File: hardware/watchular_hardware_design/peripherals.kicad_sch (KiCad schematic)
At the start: 51 parts, among them J3 TSW-116-07-H-S, J4 TSW-116-07-H-S, Q1 BSS123, Q2 BSS123, Q3 BSS123, Q4 BSS123

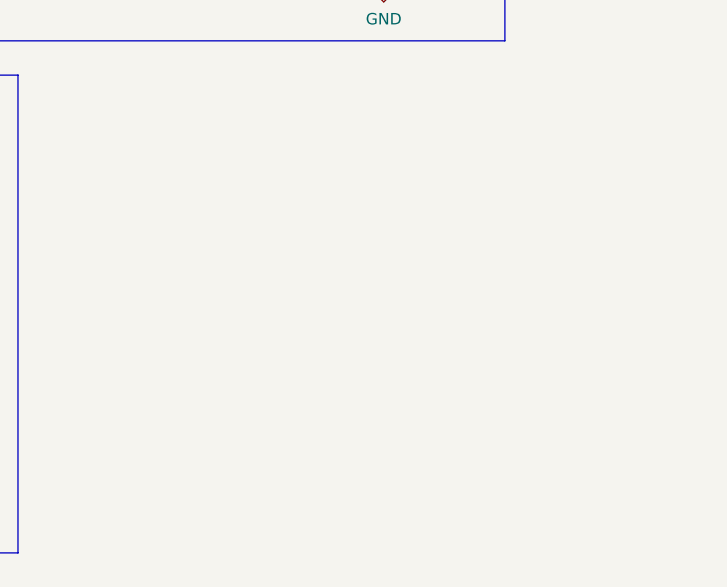
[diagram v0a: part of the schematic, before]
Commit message: Added mouting holes and assigned footprints.
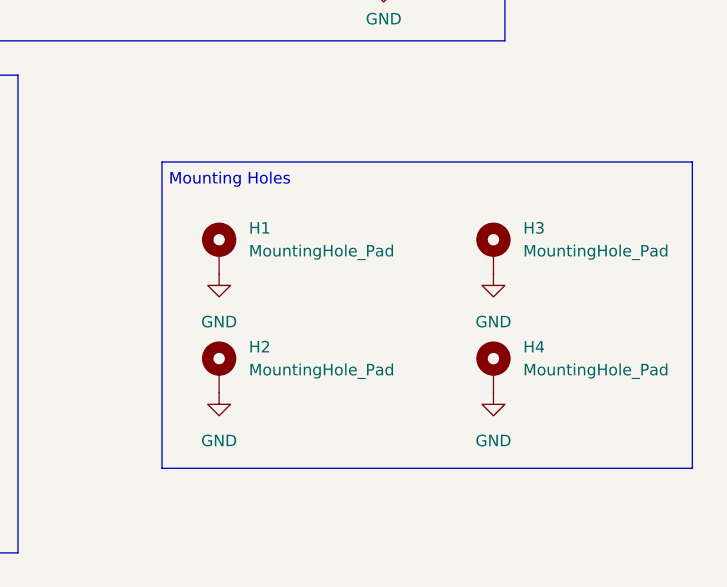
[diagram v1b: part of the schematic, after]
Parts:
- added H1, H2, H3, H4: MountingHole_Pad, MountingHole:MountingHole_4.3mm_M4_Pad_Via, symbol Mechanical:MountingHole_Pad
- J3, J4: footprint SAMTEC_TSW-116-07-H-S -> header-TSW-116-07-H-S:SAMTEC_TSW-116-07-H-S
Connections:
- net GND: now also H1.1, H2.1, H3.1, H4.1
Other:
- note added: "Mounting Holes"
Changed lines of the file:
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@@
+    (stroke (width 0) (type default) (color 0 0 0 0))
+  )
+  (polyline (pts (xy 224.028 149.606) (xy 224.028 115.57))
     (stroke (width 0) (type default) (color 0 0 0 0))
   )
@@
     (stroke (width 0) (type default) (color 0 0 0 0))
   )
+  (polyline (pts (xy 224.028 115.57) (xy 282.956 115.57))
+    (stroke (width 0) (type default) (color 0 0 0 0))
+  )
   (wire (pts (xy 35.814 58.928) (xy 39.624 58.928))
     (stroke (width 0) (type default) (color 0 0 0 0))
@@
     (stroke (width 0) (type default) (color 0 0 0 0))
   )
+  (polyline (pts (xy 282.956 149.606) (xy 224.028 149.606))
+    (stroke (width 0) (type default) (color 0 0 0 0))
+  )
   (polyline (pts (xy 76.454 116.84) (xy 76.454 160.782))
     (stroke (width 0) (type default) (color 0 0 0 0))
@@
   )
   (wire (pts (xy 248.666 69.85) (xy 248.666 78.105))
+    (stroke (width 0) (type default) (color 0 0 0 0))
+  )
+  (polyline (pts (xy 282.956 115.57) (xy 282.956 149.606))
     (stroke (width 0) (type default) (color 0 0 0 0))
   )
@@
   )
   (text "Buttons" (at 18.796 119.888 0)
+    (effects (font (size 1.27 1.27)) (justify left bottom))
+  )
+  (text "Mounting Holes" (at 224.79 118.364 0)
     (effects (font (size 1.27 1.27)) (justify left bottom))
   )
@@
     )
   )
+  (symbol (lib_id "power:GND") (at 230.378 141.224 0) (unit 1)
+    (in_bom yes) (on_board yes) (fields_autoplaced)
+    (property "Reference" "#PWR053" (id 0) (at 230.378 147.574 0)
+      (effects (font (size 1.27 1.27)) hide)
+    )
+    (property "Value" "GND" (id 1) (at 230.378 146.558 0))
+    (property "Footprint" "" (id 2) (at 230.378 141.224 0)
+      (effects (font (size 1.27 1.27)) hide)
+    )
+    (property "Datasheet" "" (id 3) (at 230.378 141.224 0)
+      (effects (font (size 1.27 1.27)) hide)
+    )
+    (pin "1")
+  )
   (symbol (lib_id "BSS123:BSS123") (at 201.422 89.916 0) (unit 1)
     (in_bom yes) (on_board yes) (fields_autoplaced)
@@
     (pin "2")
   )
+  (symbol (lib_id "power:GND") (at 260.858 128.016 0) (unit 1)
+    (in_bom yes) (on_board yes) (fields_autoplaced)
+    (property "Reference" "#PWR054" (id 0) (at 260.858 134.366 0)
+      (effects (font (size 1.27 1.27)) hide)
+    )
+    (property "Value" "GND" (id 1) (at 260.858 133.35 0))
+    (property "Footprint" "" (id 2) (at 260.858 128.016 0)
+      (effects (font (size 1.27 1.27)) hide)
+    )
+    (property "Datasheet" "" (id 3) (at 260.858 128.016 0)
+      (effects (font (size 1.27 1.27)) hide)
+    )
+    (pin "1")
+  )
   (symbol (lib_id "Device:LED") (at 191.262 42.926 180) (unit 1)
     (in_bom yes) (on_board yes)
@@
     (pin "2")
   )
+  (symbol (lib_id "Mechanical:MountingHole_Pad") (at 230.378 125.476 0) (unit 1)
+    (in_bom yes) (on_board yes) (fields_autoplaced)
+    (property "Reference" "H1" (id 0) (at 233.68 122.9359 0)
+      (effects (font (size 1.27 1.27)) (justify left))
+    )
+    (property "Value" "MountingHole_Pad" (id 1) (at 233.68 125.4759 0)
+      (effects (font (size 1.27 1.27)) (justify left))
+    )
+    (property "Footprint" "MountingHole:MountingHole_4.3mm_M4_Pad_Via" (id 2) (at 230.378 125.476 0)
+      (effects (font (size 1.27 1.27)) hide)
+    )
+    (property "Datasheet" "~" (id 3) (at 230.378 125.476 0)
+      (effects (font (size 1.27 1.27)) hide)
+    )
+    (pin "1")
+  )
   (symbol (lib_id "power:GND") (at 172.974 46.228 0) (unit 1)
     (in_bom yes) (on_board yes) (fields_autoplaced)
@@
     (pin "2")
   )
+  (symbol (lib_id "Mechanical:MountingHole_Pad") (at 260.858 125.476 0) (unit 1)
+    (in_bom yes) (on_board yes) (fields_autoplaced)
+    (property "Reference" "H3" (id 0) (at 264.16 122.9359 0)
+      (effects (font (size 1.27 1.27)) (justify left))
+    )
+    (property "Value" "MountingHole_Pad" (id 1) (at 264.16 125.4759 0)
+      (effects (font (size 1.27 1.27)) (justify left))
+    )
+    (property "Footprint" "MountingHole:MountingHole_4.3mm_M4_Pad_Via" (id 2) (at 260.858 125.476 0)
+      (effects (font (size 1.27 1.27)) hide)
+    )
+    (property "Datasheet" "~" (id 3) (at 260.858 125.476 0)
+      (effects (font (size 1.27 1.27)) hide)
+    )
+    (pin "1")
+  )
   (symbol (lib_id "Device:LED") (at 191.262 60.706 180) (unit 1)
     (in_bom yes) (on_board yes)
@@
       (effects (font (size 1.27 1.27)) (justify left) hide)
     )
-    (property "Footprint" "SAMTEC_TSW-116-07-H-S" (id 2) (at 140.462 137.668 0)
+    (property "Footprint" "header-TSW-116-07-H-S:SAMTEC_TSW-116-07-H-S" (id 2) (at 140.462 137.668 0)
       (effects (font (size 1.27 1.27)) (justify left bottom) hide)
     )
@@
     (pin "2")
   )
+  (symbol (lib_id "power:GND") (at 260.858 141.224 0) (unit 1)
+    (in_bom yes) (on_board yes) (fields_autoplaced)
+    (property "Reference" "#PWR055" (id 0) (at 260.858 147.574 0)
+      (effects (font (size 1.27 1.27)) hide)
+    )
+    (property "Value" "GND" (id 1) (at 260.858 146.558 0))
+    (property "Footprint" "" (id 2) (at 260.858 141.224 0)
+      (effects (font (size 1.27 1.27)) hide)
+    )
+    (property "Datasheet" "" (id 3) (at 260.858 141.224 0)
+      (effects (font (size 1.27 1.27)) hide)
+    )
+    (pin "1")
+  )
+  (symbol (lib_id "power:GND") (at 230.378 128.016 0) (unit 1)
+    (in_bom yes) (on_board yes) (fields_autoplaced)
+    (property "Reference" "#PWR052" (id 0) (at 230.378 134.366 0)
+      (effects (font (size 1.27 1.27)) hide)
+    )
+    (property "Value" "GND" (id 1) (at 230.378 133.35 0))
+    (property "Footprint" "" (id 2) (at 230.378 128.016 0)
+      (effects (font (size 1.27 1.27)) hide)
+    )
+    (property "Datasheet" "" (id 3) (at 230.378 128.016 0)
+      (effects (font (size 1.27 1.27)) hide)
+    )
+    (pin "1")
+  )
   (symbol (lib_id "Device:R_Small_US") (at 33.274 50.038 90) (unit 1)
     (in_bom yes) (on_board yes)
@@
     (pin "1")
     (pin "2")
+  )
+  (symbol (lib_id "Mechanical:MountingHole_Pad") (at 230.378 138.684 0) (unit 1)
+    (in_bom yes) (on_board yes) (fields_autoplaced)
+    (property "Reference" "H2" (id 0) (at 233.68 136.1439 0)
+      (effects (font (size 1.27 1.27)) (justify left))
+    )
+    (property "Value" "MountingHole_Pad" (id 1) (at 233.68 138.6839 0)
+      (effects (font (size 1.27 1.27)) (justify left))
+    )
+    (property "Footprint" "MountingHole:MountingHole_4.3mm_M4_Pad_Via" (id 2) (at 230.378 138.684 0)
+      (effects (font (size 1.27 1.27)) hide)
+    )
+    (property "Datasheet" "~" (id 3) (at 230.378 138.684 0)
+      (effects (font (size 1.27 1.27)) hide)
+    )
+    (pin "1")
   )
   (symbol (lib_id "power:GND") (at 201.422 94.996 0) (unit 1)
@@
     (pin "2")
   )
+  (symbol (lib_id "Mechanical:MountingHole_Pad") (at 260.858 138.684 0) (unit 1)
+    (in_bom yes) (on_board yes) (fields_autoplaced)
+    (property "Reference" "H4" (id 0) (at 264.16 136.1439 0)
+      (effects (font (size 1.27 1.27)) (justify left))
+    )
+    (property "Value" "MountingHole_Pad" (id 1) (at 264.16 138.6839 0)
+      (effects (font (size 1.27 1.27)) (justify left))
+    )
+    (property "Footprint" "MountingHole:MountingHole_4.3mm_M4_Pad_Via" (id 2) (at 260.858 138.684 0)
+      (effects (font (size 1.27 1.27)) hide)
+    )
+    (property "Datasheet" "~" (id 3) (at 260.858 138.684 0)
+      (effects (font (size 1.27 1.27)) hide)
+    )
+    (pin "1")
+  )
   (symbol (lib_id "Device:LED") (at 238.506 60.96 180) (unit 1)
     (in_bom yes) (on_board yes)
@@
       (effects (font (size 1.27 1.27)) (justify left) hide)
     )
-    (property "Footprint" "SAMTEC_TSW-116-07-H-S" (id 2) (at 198.12 137.668 0)
+    (property "Footprint" "header-TSW-116-07-H-S:SAMTEC_TSW-116-07-H-S" (id 2) (at 198.12 137.668 0)
       (effects (font (size 1.27 1.27)) (justify left bottom) hide)
     )

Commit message: Bottom side elements first arrangement.
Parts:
- H1, H2, H3, H4: footprint MountingHole:MountingHole_4.3mm_M4_Pad_Via -> MountingHole:MountingHole_2.2mm_M2_Pad_Via
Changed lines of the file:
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@@
       (effects (font (size 1.27 1.27)) (justify left))
     )
-    (property "Footprint" "MountingHole:MountingHole_4.3mm_M4_Pad_Via" (id 2) (at 230.378 125.476 0)
+    (property "Footprint" "MountingHole:MountingHole_2.2mm_M2_Pad_Via" (id 2) (at 230.378 125.476 0)
       (effects (font (size 1.27 1.27)) hide)
     )
@@
       (effects (font (size 1.27 1.27)) (justify left))
     )
-    (property "Footprint" "MountingHole:MountingHole_4.3mm_M4_Pad_Via" (id 2) (at 260.858 125.476 0)
+    (property "Footprint" "MountingHole:MountingHole_2.2mm_M2_Pad_Via" (id 2) (at 260.858 125.476 0)
       (effects (font (size 1.27 1.27)) hide)
     )
@@
       (effects (font (size 1.27 1.27)) (justify left))
     )
-    (property "Footprint" "MountingHole:MountingHole_4.3mm_M4_Pad_Via" (id 2) (at 230.378 138.684 0)
+    (property "Footprint" "MountingHole:MountingHole_2.2mm_M2_Pad_Via" (id 2) (at 230.378 138.684 0)
       (effects (font (size 1.27 1.27)) hide)
     )
@@
       (effects (font (size 1.27 1.27)) (justify left))
     )
-    (property "Footprint" "MountingHole:MountingHole_4.3mm_M4_Pad_Via" (id 2) (at 260.858 138.684 0)
-      (effects (font (size 1.27 1.27)) hide)
-    )
+    (property "Footprint" "MountingHole:MountingHole_2.2mm_M2_Pad_Via" (id 2) (at 260.858 138.684 0)
+      (effects (font (size 1.27 1.27)) hide)
+    )

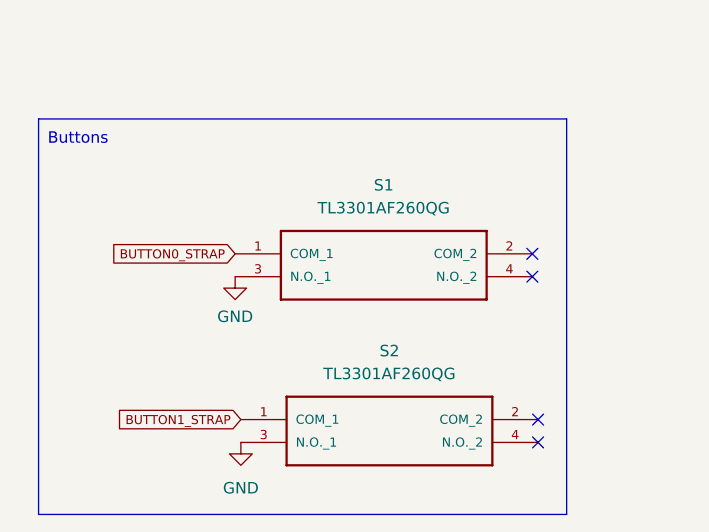
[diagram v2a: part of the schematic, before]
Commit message: Imported a bit smaller buttons.
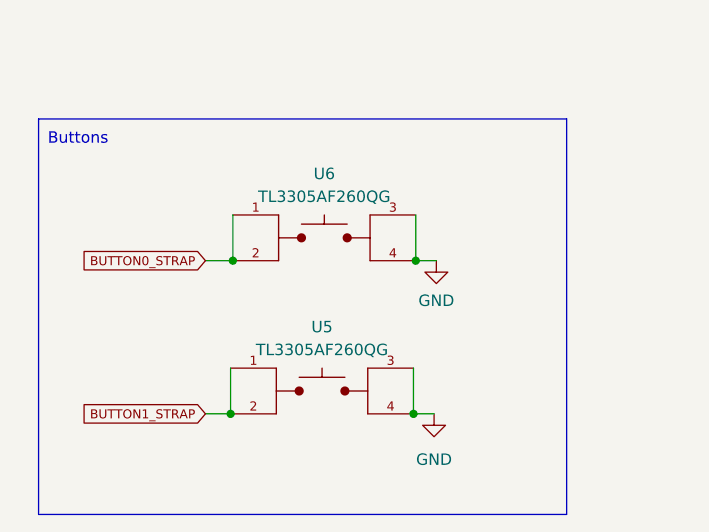
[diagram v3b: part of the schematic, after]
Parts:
- removed S1, S2: TL3301AF260QG, switch-TL3301AF260QG:TL3301AF260QG, symbol TL3301AF260QG:TL3301AF260QG
- added U5, U6: TL3305AF260QG, button_TL3305AF260QG:SW_TL3305AF260QG, symbol TL3305AF260QG:TL3305AF260QG
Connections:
- net BUTTON0_STRAP: now also U6.1, U6.2
- net BUTTON1_STRAP: now also U5.1, U5.2
- net GND: now also U5.3, U5.4, U6.3, U6.4
- no-connect marks 4 -> 0

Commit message: Locked the first digit.
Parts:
- removed H3, H4: MountingHole_Pad, MountingHole:MountingHole_2.2mm_M2_Pad_Via, symbol Mechanical:MountingHole_Pad
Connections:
- net +5V: now also J3.15; no longer J3.01
- net +BATT: now also J4.16; no longer J4.01
- net A_MCU: now also J3.02; no longer J3.04
- net BUTTON0_STRAP: now also J3.04; no longer J3.06
- net BUTTON1_STRAP: now also J3.12; no longer J3.14
- net B_MCU: now also J3.03; no longer J3.05
- net CHIP_EN: now also J3.05; no longer J3.07
- net CS-memory: now also J4.11; no longer J4.12
- net C_MCU: now also J3.07; no longer J3.09
- net DI-memory: now also J4.09; no longer J4.10
- net DIGI0: now also J4.04; no longer J4.05
- net DIGI1: now also J3.06; no longer J3.08
- net DIGI2: now also J3.14; no longer J3.16
- net DIGI3_STRAP: now also J3.13; no longer J3.15
- net DIV0-with_no_internal_flash_ONLY: now also J4.13; no longer J4.14
- net DIV1-with_no_internal_flash_ONLY: now also J4.12; no longer J4.13
- net DO-memory: now also J4.08; no longer J4.09
- net D_MCU: now also J3.08; no longer J3.10
- net E_MCU: now also J3.10; no longer J3.12
- net F_MCU: now also J3.11; no longer J3.13
- net GND: now also J3.16; no longer J3.02
- net GPIO11-to_breakout-TEST_ONLY: now also J4.14; no longer J4.15
- net G_MCU: now also J4.05; no longer J4.06
- net SPICLK-memory: now also J4.10; no longer J4.11
- net USB_D+: now also J4.06; no longer J4.07
- net USB_D-: now also J4.07; no longer J4.08
- net VDD3P3: now also J3.01; no longer J3.03
- net VDD3P3_CPU: now also J4.15; no longer J4.16
- net VDD3P3_RTC: now also J3.09; no longer J3.11
- net VDDA: now also J4.01; no longer J4.02
- net XTAL_N: now also J4.03; no longer J4.04
- net XTAL_P: now also J4.02; no longer J4.03

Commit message: Figuring out the top side...
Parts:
- R11, R12, R13, R14, R15, R16, R17, R20, R21: footprint Resistor_SMD:R_0402_1005Metric_Pad0.72x0.64mm_HandSolder -> Resistor_SMD:R_0603_1608Metric_Pad0.98x0.95mm_HandSolder
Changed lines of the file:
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@@
       (effects (font (size 1.27 1.27)) (justify left))
     )
-    (property "Footprint" "Resistor_SMD:R_0402_1005Metric_Pad0.72x0.64mm_HandSolder" (id 2) (at 156.972 61.722 0)
+    (property "Footprint" "Resistor_SMD:R_0603_1608Metric_Pad0.98x0.95mm_HandSolder" (id 2) (at 156.972 61.722 0)
       (effects (font (size 1.27 1.27)) hide)
     )
@@
       (effects (font (size 1.27 1.27)) (justify left))
     )
-    (property "Footprint" "Resistor_SMD:R_0402_1005Metric_Pad0.72x0.64mm_HandSolder" (id 2) (at 156.718 43.942 0)
+    (property "Footprint" "Resistor_SMD:R_0603_1608Metric_Pad0.98x0.95mm_HandSolder" (id 2) (at 156.718 43.942 0)
       (effects (font (size 1.27 1.27)) hide)
     )
@@
       (effects (font (size 1.27 1.27)) (justify left))
     )
-    (property "Footprint" "Resistor_SMD:R_0402_1005Metric_Pad0.72x0.64mm_HandSolder" (id 2) (at 33.274 76.708 0)
+    (property "Footprint" "Resistor_SMD:R_0603_1608Metric_Pad0.98x0.95mm_HandSolder" (id 2) (at 33.274 76.708 0)
       (effects (font (size 1.27 1.27)) hide)
     )
@@
       (effects (font (size 1.27 1.27)) (justify left))
     )
-    (property "Footprint" "Resistor_SMD:R_0402_1005Metric_Pad0.72x0.64mm_HandSolder" (id 2) (at 33.274 41.783 0)
+    (property "Footprint" "Resistor_SMD:R_0603_1608Metric_Pad0.98x0.95mm_HandSolder" (id 2) (at 33.274 41.783 0)
       (effects (font (size 1.27 1.27)) hide)
     )
@@
       (effects (font (size 1.27 1.27)) (justify left))
     )
-    (property "Footprint" "Resistor_SMD:R_0402_1005Metric_Pad0.72x0.64mm_HandSolder" (id 2) (at 33.274 33.528 0)
+    (property "Footprint" "Resistor_SMD:R_0603_1608Metric_Pad0.98x0.95mm_HandSolder" (id 2) (at 33.274 33.528 0)
       (effects (font (size 1.27 1.27)) hide)
     )
@@
       (effects (font (size 1.27 1.27)) (justify left))
     )
-    (property "Footprint" "Resistor_SMD:R_0402_1005Metric_Pad0.72x0.64mm_HandSolder" (id 2) (at 33.274 50.038 0)
+    (property "Footprint" "Resistor_SMD:R_0603_1608Metric_Pad0.98x0.95mm_HandSolder" (id 2) (at 33.274 50.038 0)
       (effects (font (size 1.27 1.27)) hide)
     )
@@
       (effects (font (size 1.27 1.27)) (justify left))
     )
-    (property "Footprint" "Resistor_SMD:R_0402_1005Metric_Pad0.72x0.64mm_HandSolder" (id 2) (at 33.274 25.273 0)
+    (property "Footprint" "Resistor_SMD:R_0603_1608Metric_Pad0.98x0.95mm_HandSolder" (id 2) (at 33.274 25.273 0)
       (effects (font (size 1.27 1.27)) hide)
     )
@@
       (effects (font (size 1.27 1.27)) (justify left))
     )
-    (property "Footprint" "Resistor_SMD:R_0402_1005Metric_Pad0.72x0.64mm_HandSolder" (id 2) (at 33.274 58.928 0)
+    (property "Footprint" "Resistor_SMD:R_0603_1608Metric_Pad0.98x0.95mm_HandSolder" (id 2) (at 33.274 58.928 0)
       (effects (font (size 1.27 1.27)) hide)
     )
@@
       (effects (font (size 1.27 1.27)) (justify left))
     )
-    (property "Footprint" "Resistor_SMD:R_0402_1005Metric_Pad0.72x0.64mm_HandSolder" (id 2) (at 33.274 68.453 0)
-      (effects (font (size 1.27 1.27)) hide)
-    )
+    (property "Footprint" "Resistor_SMD:R_0603_1608Metric_Pad0.98x0.95mm_HandSolder" (id 2) (at 33.274 68.453 0)
+      (effects (font (size 1.27 1.27)) hide)
+    )

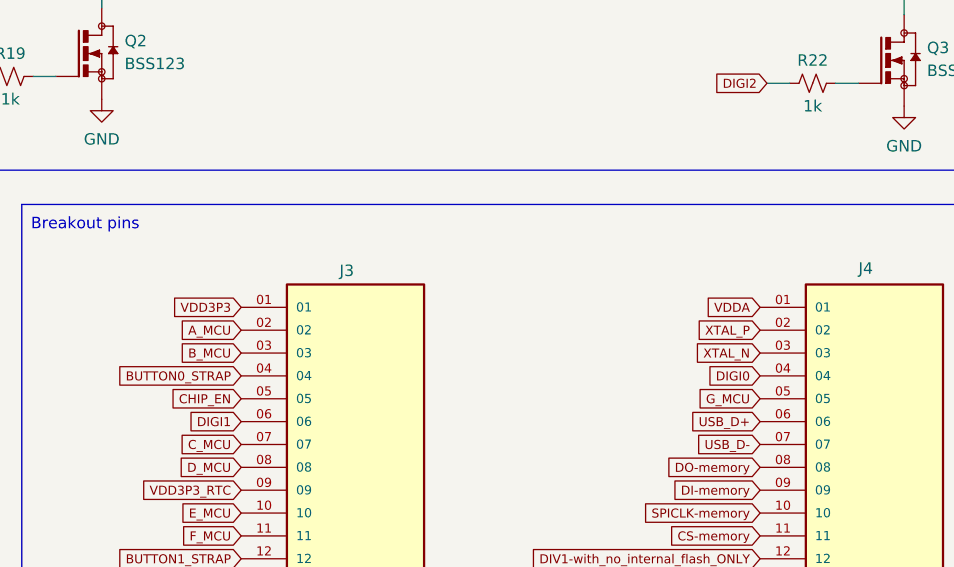
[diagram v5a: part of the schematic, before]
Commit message: Removed the filtering circuit for the VDDA to save space.
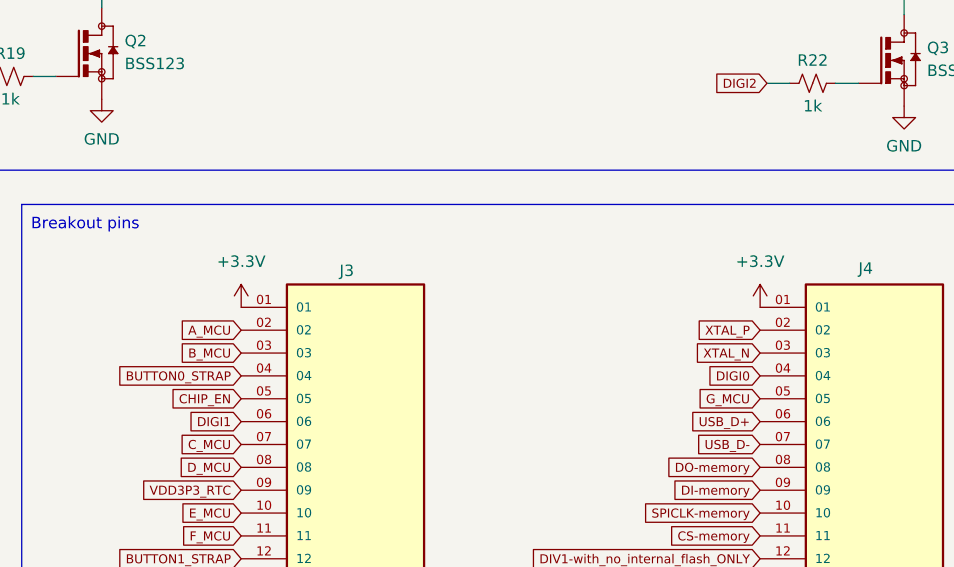
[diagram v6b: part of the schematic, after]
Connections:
- net VDDA is gone; now on net +3V3: J4.01
- net VDD3P3 renamed +3V3
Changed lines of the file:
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@@
-    )
-  )
-  (global_label "VDDA" (shape input) (at 185.42 117.348 180) (fields_autoplaced)
-    (effects (font (size 1 1)) (justify right))
-    (property "Intersheet References" "${INTERSHEET_REFS}" (id 0) (at 179.8057 117.2855 0)
-      (effects (font (size 1 1)) (justify right) hide)
     )
   )
@@
     )
   )
-  (global_label "VDD3P3" (shape input) (at 127.762 117.348 180) (fields_autoplaced)
-    (effects (font (size 1 1)) (justify right))
-    (property "Intersheet References" "${INTERSHEET_REFS}" (id 0) (at 120.1001 117.4105 0)
-      (effects (font (size 1 1)) (justify right) hide)
-    )
-  )
   (global_label "A" (shape input) (at 27.559 25.273 180) (fields_autoplaced)
     (effects (font (size 1 1)) (justify right))
@@
     (pin "2")
   )
+  (symbol (lib_id "power:+3.3V") (at 185.42 117.348 0) (unit 1)
+    (in_bom yes) (on_board yes) (fields_autoplaced)
+    (property "Reference" "#PWR0102" (id 0) (at 185.42 121.158 0)
+      (effects (font (size 1.27 1.27)) hide)
+    )
+    (property "Value" "+3.3V" (id 1) (at 185.42 112.268 0))
+    (property "Footprint" "" (id 2) (at 185.42 117.348 0)
+      (effects (font (size 1.27 1.27)) hide)
+    )
+    (property "Datasheet" "" (id 3) (at 185.42 117.348 0)
+      (effects (font (size 1.27 1.27)) hide)
+    )
+    (pin "1")
+  )
   (symbol (lib_id "Device:R_Small_US") (at 156.972 61.722 90) (unit 1)
     (in_bom yes) (on_board yes)
@@
       (effects (font (size 1.27 1.27)) hide)
     )
+    (pin "1")
+  )
+  (symbol (lib_id "power:+3.3V") (at 127.762 117.348 0) (unit 1)
+    (in_bom yes) (on_board yes) (fields_autoplaced)
+    (property "Reference" "#PWR0101" (id 0) (at 127.762 121.158 0)
+      (effects (font (size 1.27 1.27)) hide)
+    )
+    (property "Value" "+3.3V" (id 1) (at 127.762 112.268 0))
+    (property "Footprint" "" (id 2) (at 127.762 117.348 0)
+      (effects (font (size 1.27 1.27)) hide)
+    )
+    (property "Datasheet" "" (id 3) (at 127.762 117.348 0)
+      (effects (font (size 1.27 1.27)) hide)
+    )
